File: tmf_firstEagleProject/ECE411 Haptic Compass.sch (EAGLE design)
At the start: 15 parts, among them Q1 PBHV8115TLHR, Q2 PBHV8115TLHR, Q3 PBHV8115TLHR, Q4 PBHV8115TLHR, U1 328P

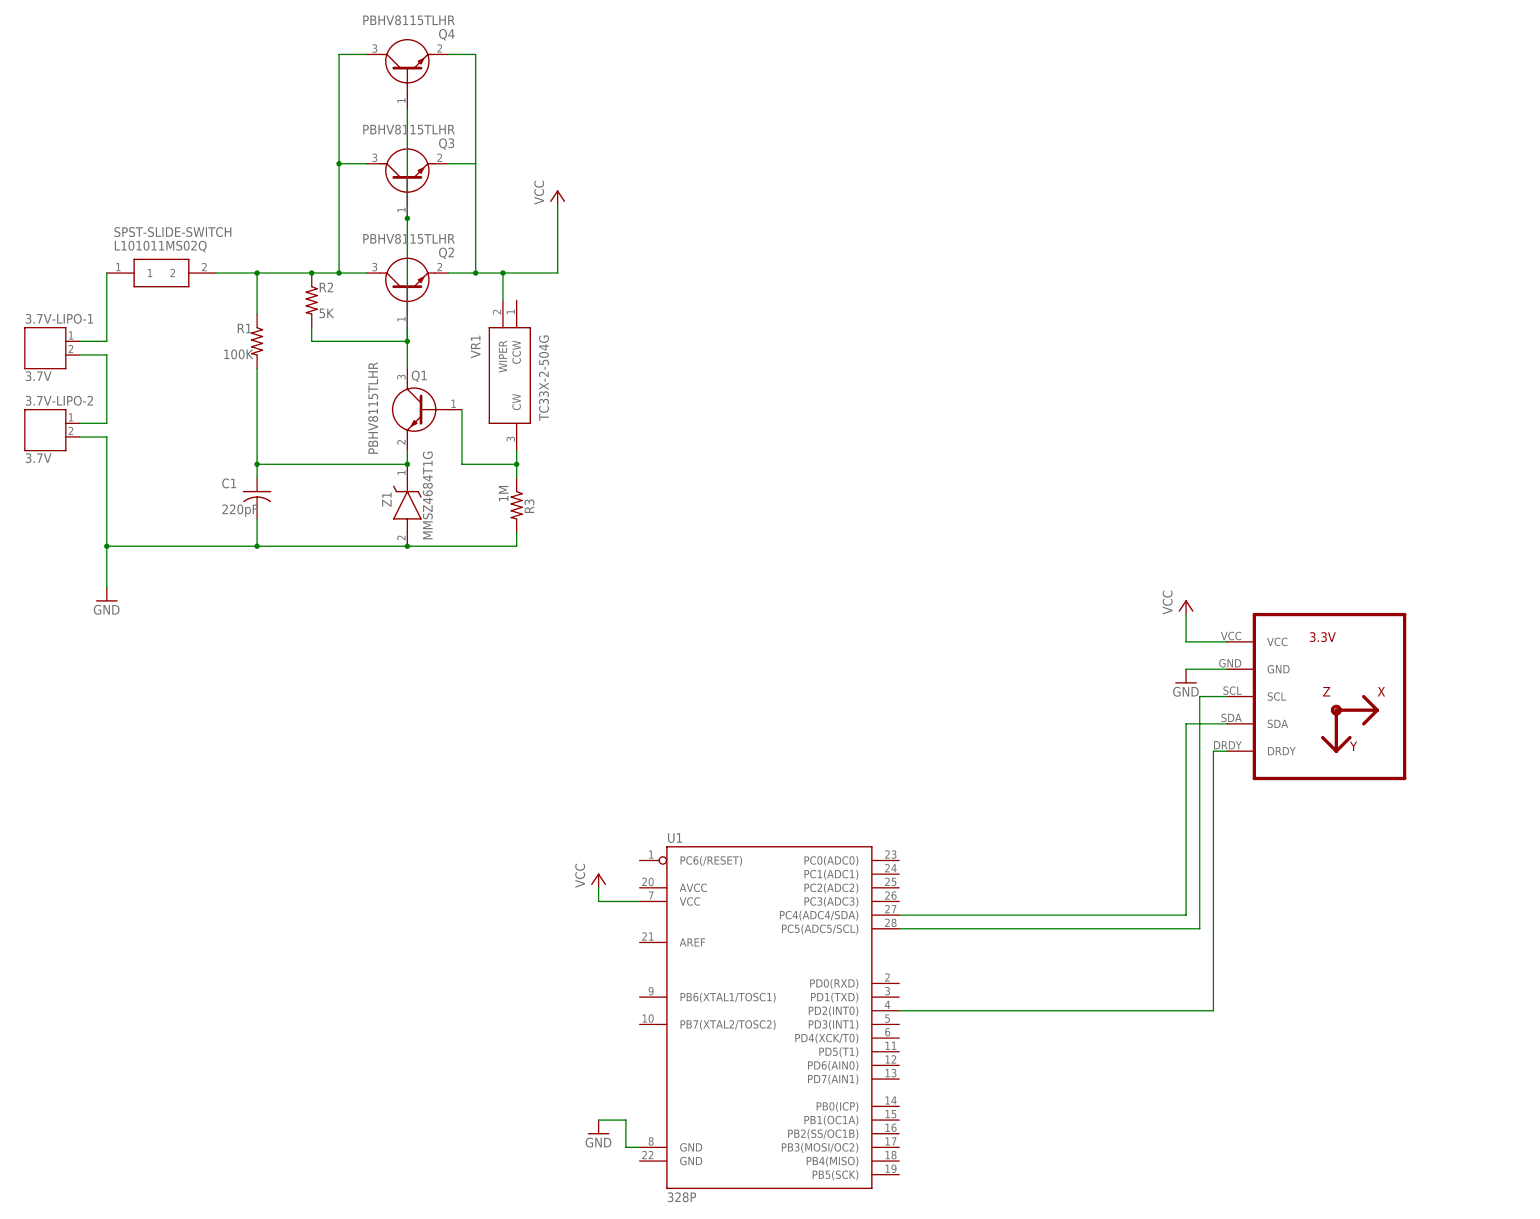
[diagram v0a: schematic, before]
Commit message: Added Reworked Power Supply for 5V
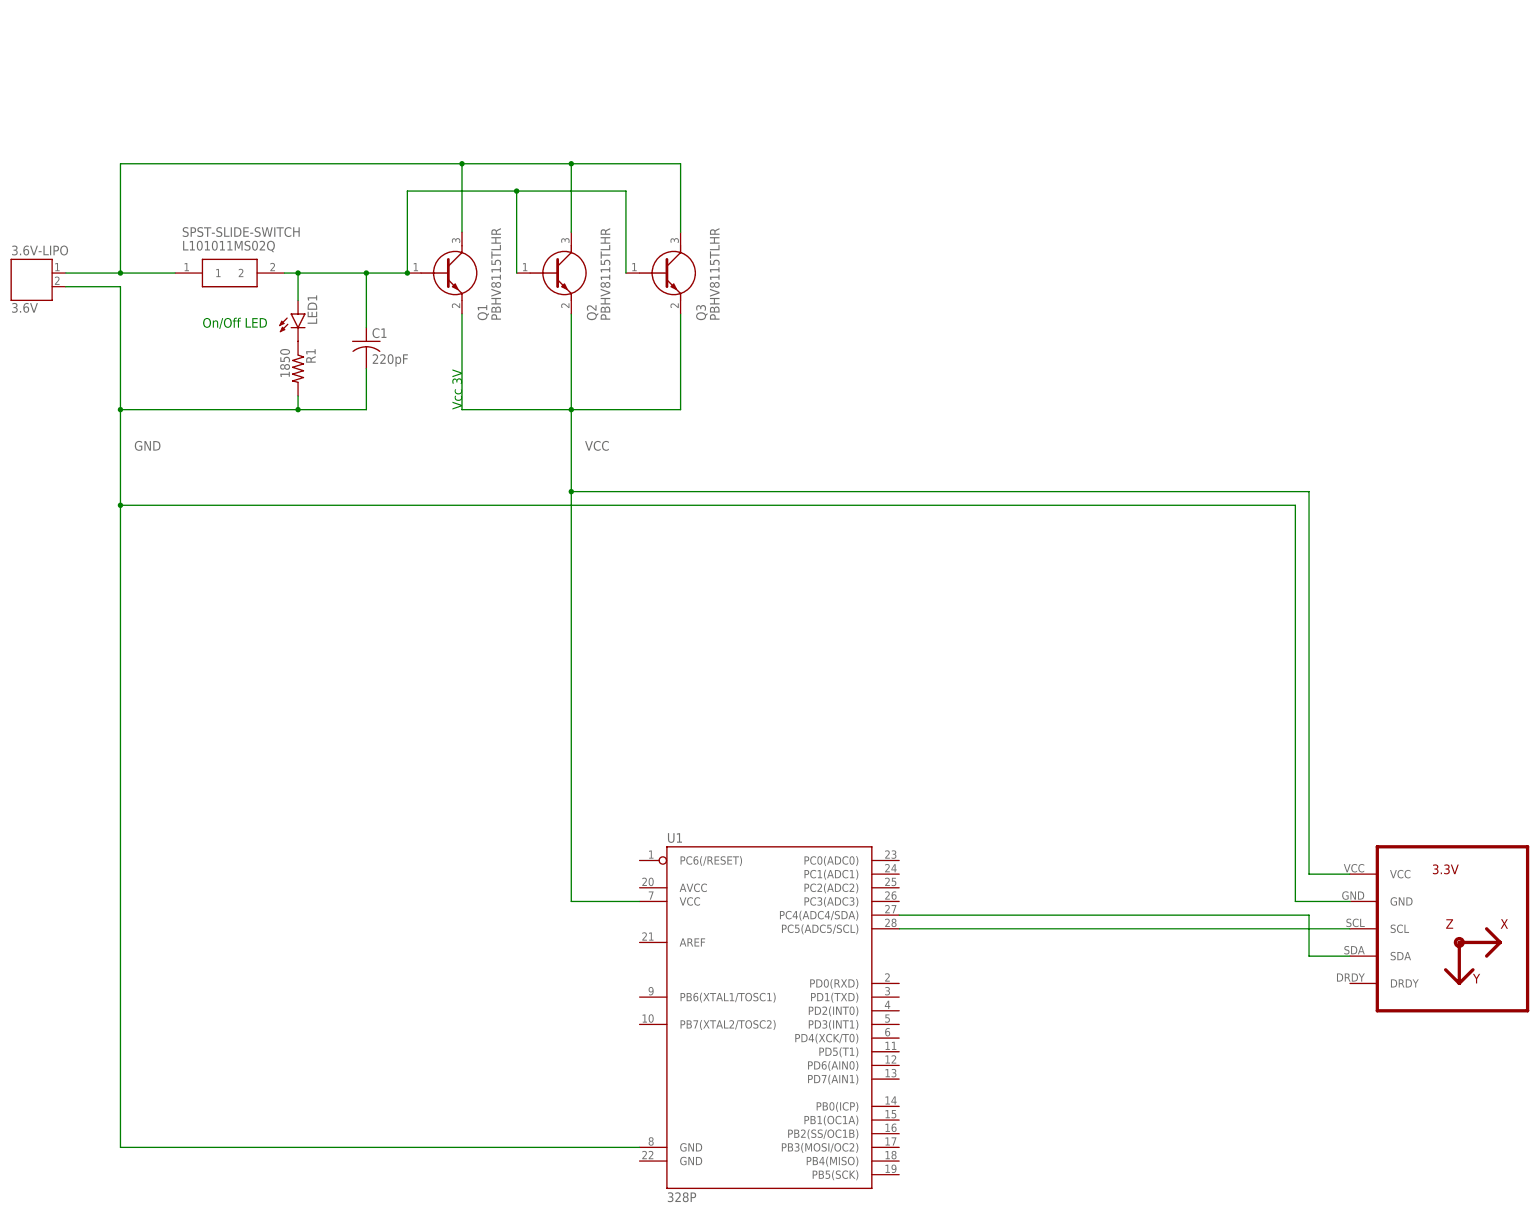
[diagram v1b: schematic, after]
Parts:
- removed 3.7V-LIPO-1, 3.7V-LIPO-2: 3.7V, jst-ph:JST-PH2
- removed Q4: PBHV8115TLHR, SamacSys_Parts:PBHV8115TLHR
- removed R2: 5K, rcl:R-US_R0805
- removed R3: 1M, rcl:R-US_R0805
- removed VR1: TC33X-2-504G, SamacSys_Parts:TC33X-2-504G
- removed Z1: MMSZ4684T1G, SamacSys_Parts:MMSZ4684T1G
- added 3.6V-LIPO: 3.6V, jst-ph:JST-PH2
- added LED1: (no value), led:LEDCHIP-LED0805
- R1: value 100K -> 1850
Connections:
- removed net N$10: 3.7V-LIPO-1.1, SPST-SLIDE-SWITCH.1
- removed net N$11: C1.1, Q1.E, R1.2, Z1.K
- removed net N$6: 3.7V-LIPO-1.2, 3.7V-LIPO-2.1
- removed net N$8: Q2.C, Q3.C, Q4.C, R1.1, R2.1, SPST-SLIDE-SWITCH.2
- removed net N$9: Q1.C, Q2.B, Q3.B, Q4.B, R2.2
- new net N$5: C1.1, LED1.A, Q1.B, Q2.B, Q3.B, SPST-SLIDE-SWITCH.2
- net GND: now also 3.6V-LIPO.2, R1.2; no longer 3.7V-LIPO-2.2, R3.2, Z1.A
- net N$3: now also LED1.C, R1.1; no longer Q1.B, R3.1, VR1.CW
- net N$4: now also 3.6V-LIPO.1, Q1.C, Q2.C, Q3.C, SPST-SLIDE-SWITCH.1; no longer MAGNETOMETER.DRDY, U1.PD2(INT0)
- net VCC: now also Q1.E; no longer Q4.E, VR1.WIPER
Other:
- note added: "On/Off LED"
- note added: "Vcc 3V"
- moved on the sheet: C1, Q1, Q2, Q3, R1, SPST-SLIDE-SWITCH
